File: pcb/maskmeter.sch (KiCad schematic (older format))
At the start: 12 parts, among them SW1 SW_Push, U1 TLC555IDR

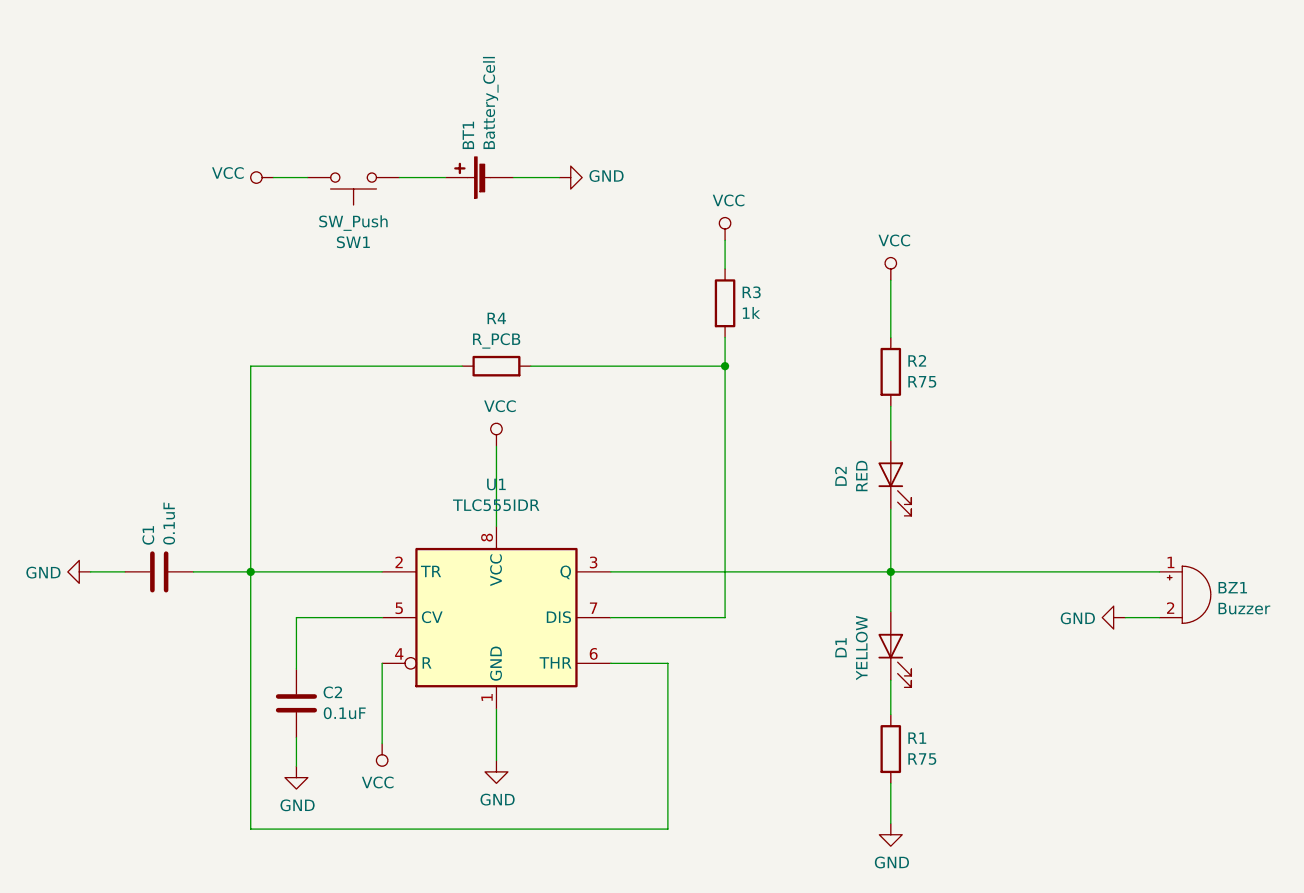
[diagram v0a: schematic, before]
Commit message: Changed resitors and green LED
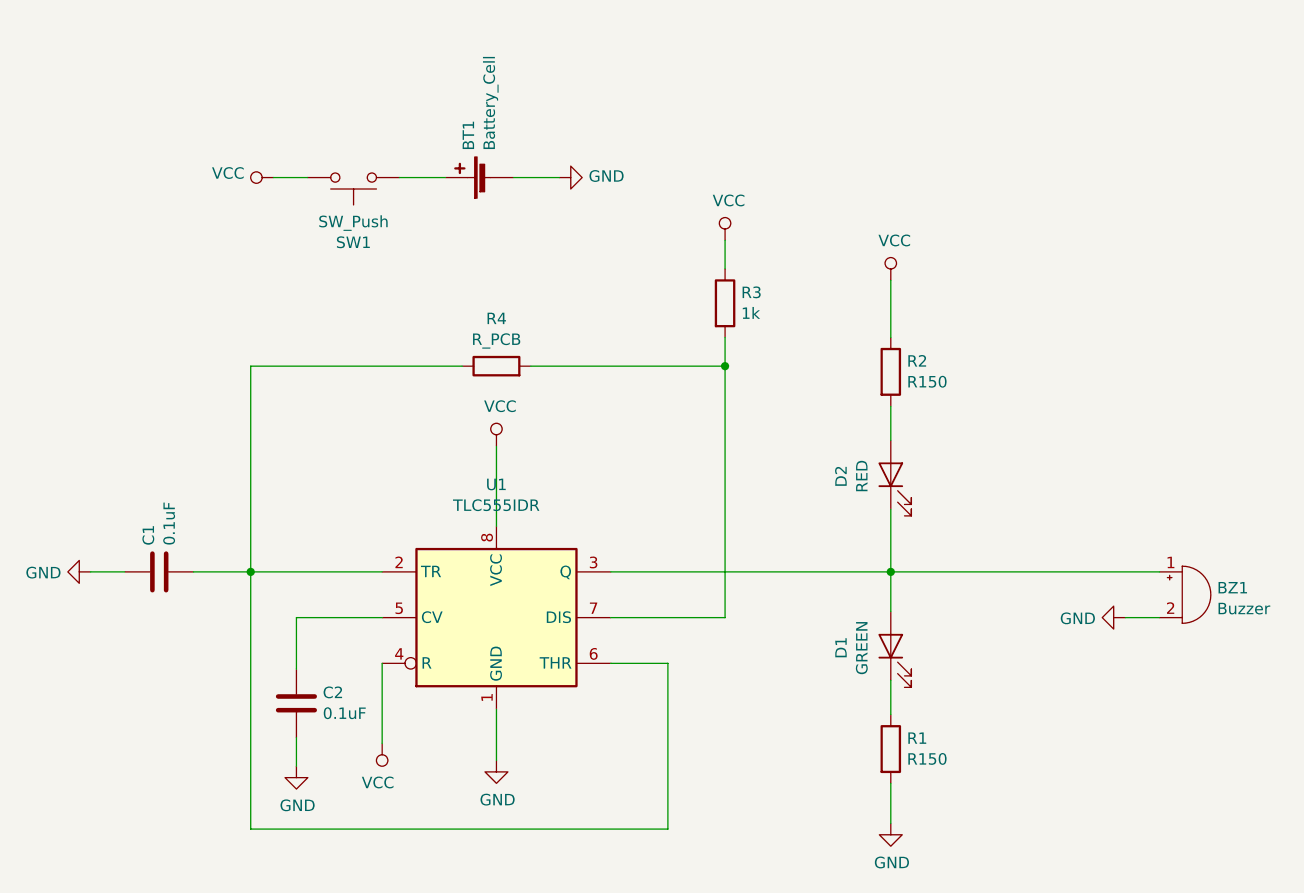
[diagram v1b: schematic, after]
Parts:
- D1: value YELLOW -> GREEN; LCSC C2296 -> C375452
- R1, R2: value R75 -> R150; LCSC C4275 -> C22808
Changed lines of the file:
@@
 P 6700 4400
 F 0 "R1" H 6770 4446 50  0000 L CNN
-F 1 "R75" H 6770 4355 50  0000 L CNN
+F 1 "R150" H 6770 4355 50  0000 L CNN
 F 2 "Resistor_SMD:R_0603_1608Metric" V 6630 4400 50  0001 C CNN
 F 3 "~" H 6700 4400 50  0001 C CNN
-F 4 "C4275" H 6700 4400 50  0001 C CNN "LCSC"
+F 4 "C22808" H 6700 4400 50  0001 C CNN "LCSC"
 	1    6700 4400
 	1    0    0    -1
@@
 P 6700 2750
 F 0 "R2" H 6770 2796 50  0000 L CNN
-F 1 "R75" H 6770 2705 50  0000 L CNN
+F 1 "R150" H 6770 2705 50  0000 L CNN
 F 2 "Resistor_SMD:R_0603_1608Metric" V 6630 2750 50  0001 C CNN
 F 3 "~" H 6700 2750 50  0001 C CNN
-F 4 "C4275" H 6700 2750 50  0001 C CNN "LCSC"
+F 4 "C22808" H 6700 2750 50  0001 C CNN "LCSC"
 	1    6700 2750
 	1    0    0    -1
@@
 P 6700 3950
 F 0 "D1" H 6693 4166 50  0000 C CNN
-F 1 "YELLOW" H 6693 4075 50  0000 C CNN
+F 1 "GREEN" H 6693 4075 50  0000 C CNN
 F 2 "LED_SMD:LED_0805_2012Metric_Castellated" H 6700 3950 50  0001 C CNN
 F 3 "~" H 6700 3950 50  0001 C CNN
-F 4 "C2296" H 6700 3950 50  0001 C CNN "LCSC"
+F 4 "C375452" H 6700 3950 50  0001 C CNN "LCSC"
 	1    6700 3950
 	0    -1   -1   0
